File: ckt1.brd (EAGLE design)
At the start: 100 x 63.5 mm, 16 parts, among them J1 POWER_JACKSLT, M1 WIRELESS-NRF24L01-PA-EXT, U1 328P

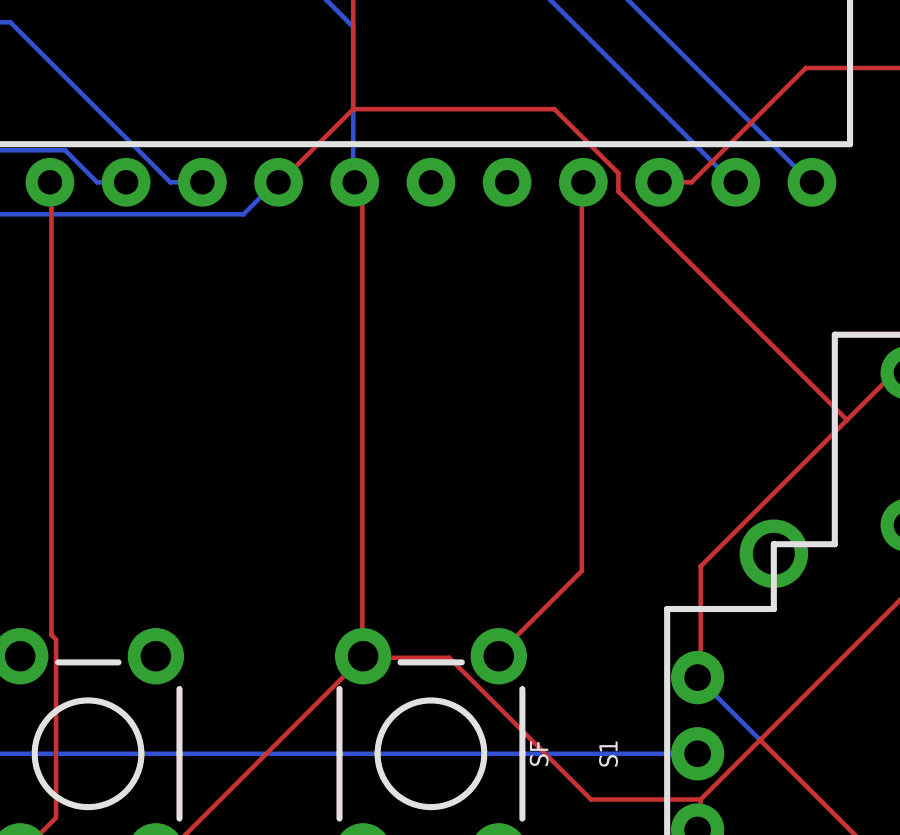
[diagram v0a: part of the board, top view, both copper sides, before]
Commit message: Formatting schematic and adding XTAL
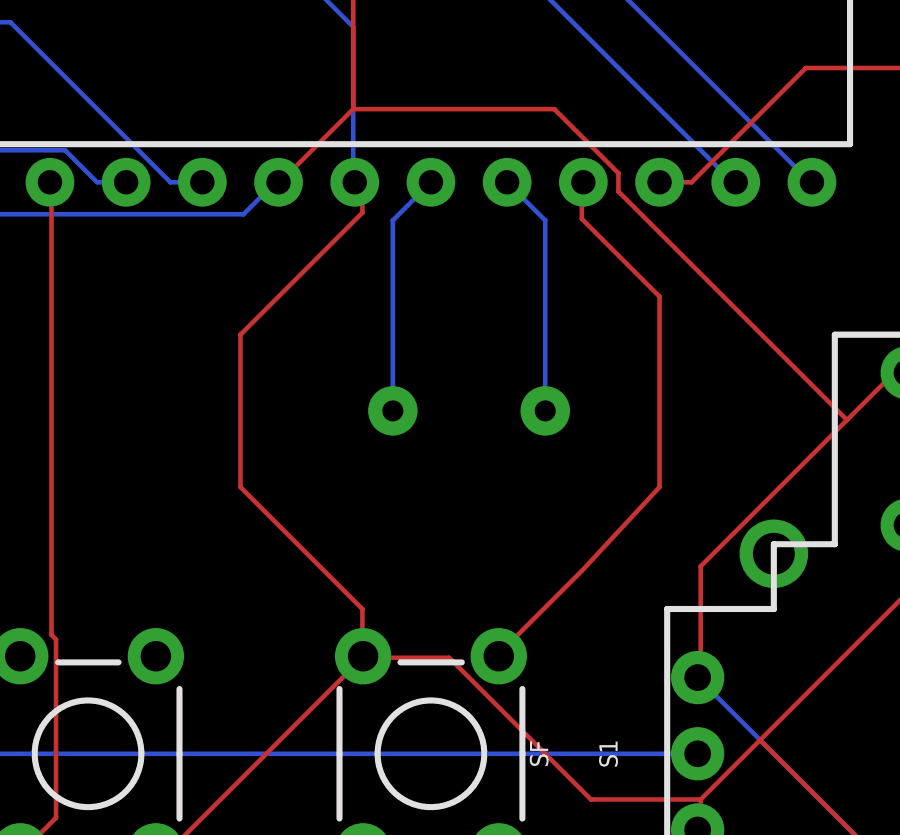
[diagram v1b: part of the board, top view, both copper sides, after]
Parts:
- added Y1: (no value), SparkFun-Clocks:HC49US
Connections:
- new net N$1: U1.9, Y1.2
- new net N$3: U1.10, Y1.1
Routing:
- net N$3: track 0.00 -> 8.15 mm
- net N$1: track 0.00 -> 8.15 mm
- net GND: track 246.2 -> 249.6 mm
- net PD5: track 17.0 -> 19.1 mm
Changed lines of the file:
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@@
 <attribute name="VALUE" x="72.39" y="38.1" size="0.6096" layer="27" font="vector" ratio="20" rot="R90" align="bottom-center"/>
+</element>
+<element name="Y1" library="SparkFun-Clocks" package="HC49US" value="" x="58.42" y="26.67" smashed="yes" rot="MR0">
+<attribute name="NAME" x="58.42" y="29.21" size="0.6096" layer="26" font="vector" ratio="20" rot="MR0" align="bottom-center"/>
+<attribute name="VALUE" x="58.42" y="24.13" size="0.6096" layer="28" font="vector" ratio="20" rot="MR0" align="top-center"/>
 </element>
 </elements>
@@
 <wire x1="39.7764" y1="47.7012" x2="41.6052" y2="49.53" width="0.1524" layer="1"/>
 <wire x1="30.1752" y1="47.7012" x2="39.7764" y2="47.7012" width="0.1524" layer="1"/>
-<wire x1="54.864" y1="34.1376" x2="54.864" y2="18.5928" width="0.1524" layer="1"/>
+<wire x1="54.864" y1="34.1376" x2="54.864" y2="33.274" width="0.1524" layer="1"/>
+<wire x1="54.864" y1="33.274" x2="50.8" y2="29.21" width="0.1524" layer="1"/>
+<wire x1="50.8" y1="29.21" x2="50.8" y2="24.13" width="0.1524" layer="1"/>
+<wire x1="50.8" y1="24.13" x2="54.864" y2="20.066" width="0.1524" layer="1"/>
+<wire x1="54.864" y1="20.066" x2="54.864" y2="18.5928" width="0.1524" layer="1"/>
 <wire x1="54.7116" y1="34.29" x2="54.864" y2="34.1376" width="0.1524" layer="1"/>
 <wire x1="54.864" y1="18.5928" x2="54.8894" y2="18.4912" width="0.1524" layer="1"/>
@@
 <contactref element="SF" pad="1"/>
 <contactref element="U1" pad="11"/>
-<wire x1="62.1792" y1="21.336" x2="62.1792" y2="34.29" width="0.1524" layer="1"/>
+<wire x1="62.1792" y1="21.336" x2="64.77" y2="24.13" width="0.1524" layer="1"/>
+<wire x1="64.77" y1="24.13" x2="64.77" y2="30.48" width="0.1524" layer="1"/>
+<wire x1="64.77" y1="30.48" x2="62.1792" y2="33.0708" width="0.1524" layer="1"/>
+<wire x1="62.1792" y1="33.0708" x2="62.1792" y2="34.29" width="0.1524" layer="1"/>
 <wire x1="59.436" y1="18.5928" x2="62.1792" y2="21.336" width="0.1524" layer="1"/>
 <wire x1="62.1792" y1="34.29" x2="62.23" y2="34.29" width="0.1524" layer="1"/>
@@
 <wire x1="82.55" y1="38.1" x2="69.6468" y2="38.1" width="0.1524" layer="1"/>
 </signal>
+<signal name="N$1">
+<contactref element="Y1" pad="2"/>
+<contactref element="U1" pad="9"/>
+<wire x1="55.88" y1="26.67" x2="55.88" y2="33.02" width="0.1524" layer="16"/>
+<wire x1="55.88" y1="33.02" x2="57.15" y2="34.29" width="0.1524" layer="16"/>
+</signal>
+<signal name="N$3">
+<contactref element="Y1" pad="1"/>
+<contactref element="U1" pad="10"/>
+<wire x1="60.96" y1="26.67" x2="60.96" y2="33.02" width="0.1524" layer="16"/>
+<wire x1="60.96" y1="33.02" x2="59.69" y2="34.29" width="0.1524" layer="16"/>
+</signal>
 </signals>

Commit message: Some changes to the board file
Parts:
- turned S1 to 180 degrees
- turned S2 to 180 degrees
- turned S3 to 0 degrees
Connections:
- new net PC2: S1.V2, U1.25
- new net PC3: S1.H2, U1.26
- net GND: no longer S1.B2A, S2.B2A
- net PC0: now also U1.23; no longer S1.V2
- net PC1: now also U1.24; no longer S1.H2
- net VCC: no longer S1.B1A, S2.B1A
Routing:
- net PC2: track 0.00 -> 54.7 mm
- net PC3: track 0.00 -> 43.1 mm
- net VCC: track 163.9 -> 141.3 mm
- net PC1: track 53.6 -> 32.2 mm
- net PC0: track 52.6 -> 31.7 mm
- net GND: track 249.6 -> 234.4 mm
- net PD4: track 40.4 -> 48.6 mm
- net PD5: track 19.1 -> 17.0 mm
- net PD1: track 32.9 -> 32.0 mm
- net PD3: track 27.3 -> 26.5 mm
